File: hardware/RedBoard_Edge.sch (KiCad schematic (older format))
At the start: 66 parts, among them IC3 LM1117, J1 CONN_025MM, J17 Qwiic_Connector, J18 Qwiic_Connector, J2 ICSP, J3 POWER_JACKSUPER_BOMB_DIGITY, J4 microB, J5 CONN_04, J6 CONN_04, Q1 1A/60V/500mO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

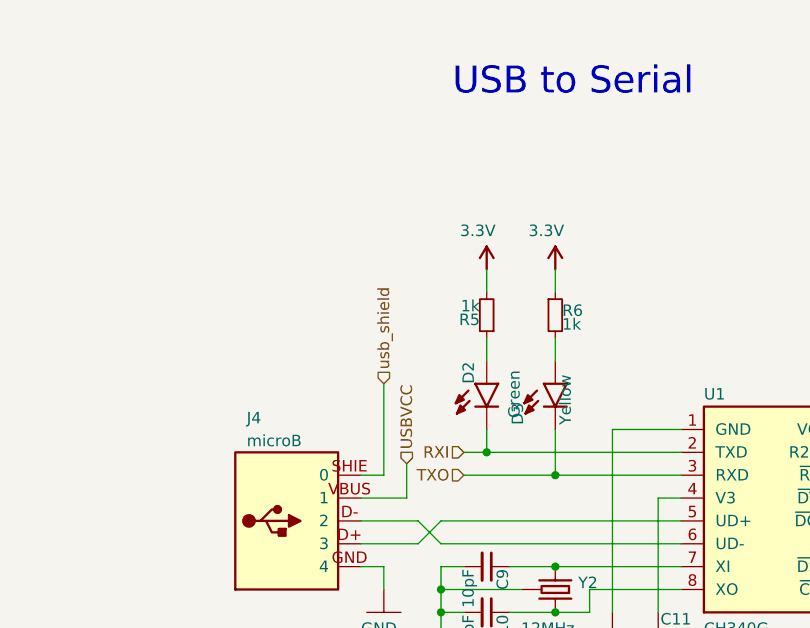
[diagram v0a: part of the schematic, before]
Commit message: Finalized Layout and ordered first run
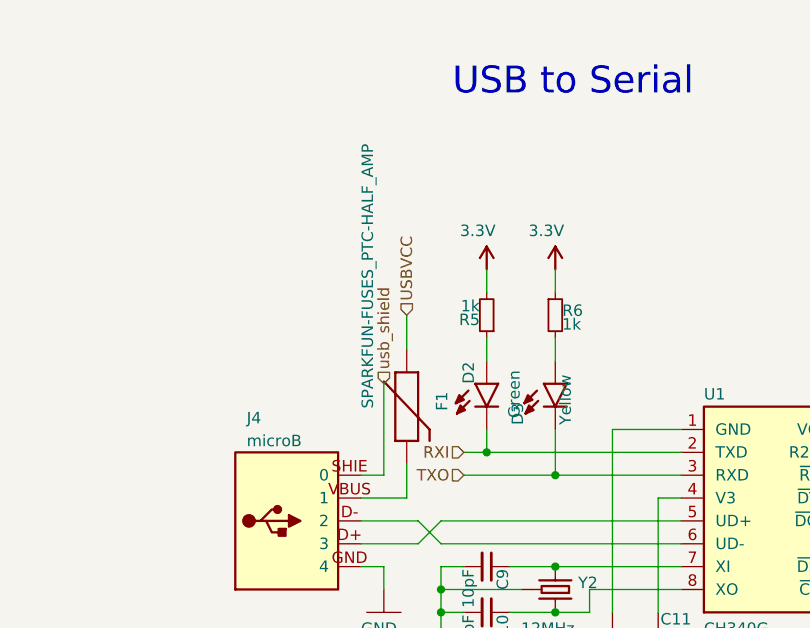
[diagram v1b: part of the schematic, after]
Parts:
- added F1: SPARKFUN-FUSES_PTC-HALF_AMP, RedBoard:SPARKFUN-FUSES_1206, symbol SPARKFUN-FUSES_PTC-HALF_AMP
- R5, R6: footprint Resistors_SMD:R_0603 -> RedBoard:SPARKFUN-RESISTORS_0603
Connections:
- net USBVCC: now also F1.1; no longer J4.VBUS (1)
- new net: F1.2, J4.VBUS (1)
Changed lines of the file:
@@
 EESchema Schematic File Version 2
-LIBS:RedBoard
 LIBS:LilyPad-Wearables
 LIBS:SparkFun-Aesthetics
@@
 LIBS:CMArduino-cache
 LIBS:RedBoard-cache
+LIBS:RedBoard_Edge
+LIBS:RedBoard
+LIBS:RedBoard_Edge-cache
 EELAYER 25 0
 EELAYER END
@@
 F 0 "R5" H 2680 1820 50  0000 L CNN
 F 1 "1k" H 2680 1760 50  0000 L CNN
-F 2 "Resistors_SMD:R_0603" H 2650 1800 50  0001 C CNN
+F 2 "RedBoard:SPARKFUN-RESISTORS_0603" H 2650 1800 50  0001 C CNN
 F 3 "" H 2650 1800 50  0001 C CNN
 	1    2650 1800
@@
 F 0 "R6" H 2980 1820 50  0000 L CNN
 F 1 "1k" H 2980 1760 50  0000 L CNN
-F 2 "Resistors_SMD:R_0603" H 2950 1800 50  0001 C CNN
+F 2 "RedBoard:SPARKFUN-RESISTORS_0603" H 2950 1800 50  0001 C CNN
 F 3 "" H 2950 1800 50  0001 C CNN
 	1    2950 1800
@@
 $EndComp
 $Comp
-L SPARKFUN_5V #U$036
+L SPARKFUN_5V #U$035
 U 1 1 595ED4F8
 P 9450 6700
-F 0 "#U$036" H 9411 6840 50  0001 L BNN
+F 0 "#U$035" H 9411 6840 50  0001 L BNN
 F 1 "5V" H 9500 6700 50  0000 L BNN
 F 2 "" H 9450 6700 60  0001 C CNN
@@
 $EndComp
 $Comp
-L SPARKFUN_3.3V #P+037
+L SPARKFUN_3.3V #P+036
 U 1 1 595ED59B
 P 9450 6900
-F 0 "#P+037" H 9411 7040 50  0001 L BNN
+F 0 "#P+036" H 9411 7040 50  0001 L BNN
 F 1 "3.3V" H 9500 6900 50  0000 L BNN
 F 2 "" H 9450 6900 60  0001 C CNN
@@
 	2100 2600 2300 2600
 Wire Wire Line
-	2300 2600 2300 2450
-Wire Wire Line
 	4750 2600 4750 2700
 Wire Wire Line
@@
 Connection ~ 3250 7200
 $Comp
-L SPARKFUN_GND #GND038
+L SPARKFUN_GND #GND037
 U 1 1 595EF22D
 P 3250 7400
-F 0 "#GND038" H 3150 7300 50  0001 L BNN
+F 0 "#GND037" H 3150 7300 50  0001 L BNN
 F 1 "GND" H 3150 7300 50  0000 L BNN
 F 2 "" H 3250 7400 60  0001 C CNN
@@
 	13550 7400 13550 7500
 $Comp
-L SPARKFUN-AESTHETICS_3.3V #SUPPLY039
+L SPARKFUN-AESTHETICS_3.3V #SUPPLY038
 U 1 1 595F2477
 P 13550 7200
-F 0 "#SUPPLY039" H 13511 7340 50  0001 L BNN
+F 0 "#SUPPLY038" H 13511 7340 50  0001 L BNN
 F 1 "3.3V" H 13511 7340 50  0000 L BNN
 F 2 "" H 13550 7200 60  0001 C CNN
@@
 $EndComp
 $Comp
-L SPARKFUN_GND #GND040
+L SPARKFUN_GND #GND039
 U 1 1 595F247D
 P 13550 7600
-F 0 "#GND040" H 13450 7500 50  0001 L BNN
+F 0 "#GND039" H 13450 7500 50  0001 L BNN
 F 1 "GND" H 13450 7500 50  0000 L BNN
 F 2 "" H 13550 7600 60  0001 C CNN
@@
 	13550 8200 13550 8300
 $Comp
-L SPARKFUN-AESTHETICS_3.3V #SUPPLY041
+L SPARKFUN-AESTHETICS_3.3V #SUPPLY040
 U 1 1 595F2491
 P 13550 8000
-F 0 "#SUPPLY041" H 13511 8140 50  0001 L BNN
+F 0 "#SUPPLY040" H 13511 8140 50  0001 L BNN
 F 1 "3.3V" H 13511 8140 50  0000 L BNN
 F 2 "" H 13550 8000 60  0001 C CNN
@@
 $EndComp
 $Comp
-L SPARKFUN_GND #GND042
+L SPARKFUN_GND #GND041
 U 1 1 595F2497
 P 13550 8400
-F 0 "#GND042" H 13450 8300 50  0001 L BNN
+F 0 "#GND041" H 13450 8300 50  0001 L BNN
 F 1 "GND" H 13450 8300 50  0000 L BNN
 F 2 "" H 13550 8400 60  0001 C CNN
@@
 $EndComp
 $Comp
-L SPARKFUN_5V #U$043
+L SPARKFUN_5V #U$042
 U 1 1 595F7886
 P 14550 7650
-F 0 "#U$043" H 14511 7790 50  0001 L BNN
+F 0 "#U$042" H 14511 7790 50  0001 L BNN
 F 1 "5V" H 14511 7790 50  0000 L BNN
 F 2 "" H 14550 7650 60  0001 C CNN
@@
 $EndComp
 $Comp
-L SPARKFUN-AESTHETICS_3.3V #SUPPLY044
+L SPARKFUN-AESTHETICS_3.3V #SUPPLY043
 U 1 1 595F7B0F
 P 14050 7650
-F 0 "#SUPPLY044" H 14011 7790 50  0001 L BNN
+F 0 "#SUPPLY043" H 14011 7790 50  0001 L BNN
 F 1 "3.3V" H 14011 7790 50  0000 L BNN
 F 2 "" H 14050 7650 60  0001 C CNN
@@
 $EndComp
 $Comp
-L SPARKFUN_5V #U$045
+L SPARKFUN_5V #U$044
 U 1 1 595F8680
 P 14550 6550
-F 0 "#U$045" H 14511 6690 50  0001 L BNN
+F 0 "#U$044" H 14511 6690 50  0001 L BNN
 F 1 "5V" H 14511 6690 50  0000 L BNN
 F 2 "" H 14550 6550 60  0001 C CNN
@@
 $EndComp
 $Comp
-L SPARKFUN-AESTHETICS_3.3V #SUPPLY046
+L SPARKFUN-AESTHETICS_3.3V #SUPPLY045
 U 1 1 595F868D
 P 14050 6550
-F 0 "#SUPPLY046" H 14011 6690 50  0001 L BNN
+F 0 "#SUPPLY045" H 14011 6690 50  0001 L BNN
 F 1 "3.3V" H 14011 6690 50  0000 L BNN
 F 2 "" H 14050 6550 60  0001 C CNN
@@
 Connection ~ 10300 6950
 $Comp
-L SPARKFUN_GND #GND047
+L SPARKFUN_GND #GND046
 U 1 1 59603275
 P 10300 7150
-F 0 "#GND047" H 10200 7050 50  0001 L BNN
+F 0 "#GND046" H 10200 7050 50  0001 L BNN
 F 1 "GND" H 10200 7050 50  0000 L BNN
 F 2 "" H 10300 7150 60  0001 C CNN
@@
 Connection ~ 4150 6700
 $Comp
-L SPARKFUN_5V #U$048
+L SPARKFUN_5V #U$047
 U 1 1 596038F0
 P 4150 6600
-F 0 "#U$048" H 4111 6740 50  0001 L BNN
+F 0 "#U$047" H 4111 6740 50  0001 L BNN
 F 1 "5V" H 4200 6600 50  0000 L BNN
 F 2 "" H 4150 6600 60  0001 C CNN
@@
 Connection ~ 3450 9850
 $Comp
-L SPARKFUN_GND #GND049
+L SPARKFUN_GND #GND048
 U 1 1 59604668
 P 3450 10050
-F 0 "#GND049" H 3350 9950 50  0001 L BNN
+F 0 "#GND048" H 3350 9950 50  0001 L BNN
 F 1 "GND" H 3350 9950 50  0000 L BNN
 F 2 "" H 3450 10050 60  0001 C CNN
@@
 Connection ~ 4150 9750
 $Comp
-L SPARKFUN_5V #U$050
+L SPARKFUN_5V #U$049
 U 1 1 59604DE3
 P 4150 9450
-F 0 "#U$050" H 4111 9590 50  0001 L BNN
+F 0 "#U$049" H 4111 9590 50  0001 L BNN
 F 1 "5V" H 4200 9450 50  0000 L BNN
 F 2 "" H 4150 9450 60  0001 C CNN
@@
 Connection ~ 7850 9750
 $Comp
-L SPARKFUN_GND #GND051
+L SPARKFUN_GND #GND050
 U 1 1 59605021
 P 7850 9950
-F 0 "#GND051" H 7750 9850 50  0001 L BNN
+F 0 "#GND050" H 7750 9850 50  0001 L BNN
 F 1 "GND" H 7750 9850 50  0000 L BNN
 F 2 "" H 7850 9950 60  0001 C CNN
@@
 Connection ~ 8550 9650
 $Comp
-L SPARKFUN_5V #U$052
+L SPARKFUN_5V #U$051
 U 1 1 59605035
 P 8550 9350
-F 0 "#U$052" H 8511 9490 50  0001 L BNN
+F 0 "#U$051" H 8511 9490 50  0001 L BNN
 F 1 "5V" H 8600 9350 50  0000 L BNN
 F 2 "" H 8550 9350 60  0001 C CNN
@@
 	10300 6650 10300 7050
 $Comp
-L SPARKFUN_GND #GND053
+L SPARKFUN_GND #GND052
 U 1 1 5960784C
 P 8600 7050
-F 0 "#GND053" H 8500 6950 50  0001 L BNN
+F 0 "#GND052" H 8500 6950 50  0001 L BNN
 F 1 "GND" H 8500 6950 50  0000 L BNN
 F 2 "" H 8600 7050 60  0001 C CNN
@@
 $EndComp
 $Comp
-L SPARKFUN-AESTHETICS_VIN #SUPPLY054
+L SPARKFUN-AESTHETICS_VIN #SUPPLY053
 U 1 1 59609021
 P 8600 6650
-F 0 "#SUPPLY054" H 8561 6790 50  0001 L BNN
+F 0 "#SUPPLY053" H 8561 6790 50  0001 L BNN
 F 1 "VIN" H 8561 6790 50  0000 L BNN
 F 2 "" H 8600 6650 60  0001 C CNN
@@
 usb_shield
 $Comp
-L SPARKFUN_GND #GND055
+L SPARKFUN_GND #GND054
 U 1 1 596B51FB
 P 6550 7200
-F 0 "#GND055" H 6450 7100 50  0001 L BNN
+F 0 "#GND054" H 6450 7100 50  0001 L BNN
 F 1 "GND" H 6450 7100 50  0000 L BNN
 F 2 "" H 6550 7200 60  0001 C CNN
@@
 Wire Wire Line
 	7350 1600 7250 1600
-Text HLabel 2300 2450 1    50   Input ~ 0
+Text HLabel 2300 1800 1    50   Input ~ 0
 USBVCC
+$Comp
+L SPARKFUN-FUSES_PTC-HALF_AMP F1
+U 1 1 5983A4D8
+P 2300 2150
+F 0 "F1" H 2285 2275 50  0000 L BNN
+F 1 "SPARKFUN-FUSES_PTC-HALF_AMP" H 1200 1950 50  0000 L BNN
+F 2 "RedBoard:SPARKFUN-FUSES_1206" H 2300 2150 50  0001 C CNN
+F 3 "" H 2300 2150 50  0001 C CNN
+	1    2300 2150
+	0    1    1    0
+$EndComp
+Wire Wire Line
+	2300 2600 2300 2450
+Wire Wire Line
+	2300 1950 2300 1800
 $EndSCHEMATC
